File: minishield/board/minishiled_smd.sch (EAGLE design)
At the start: 13 parts, among them CON1 TWIG-90-SMD, CON2 TWIG-90-SMD, U1 ARDUINO_SHIELDNO_SILK

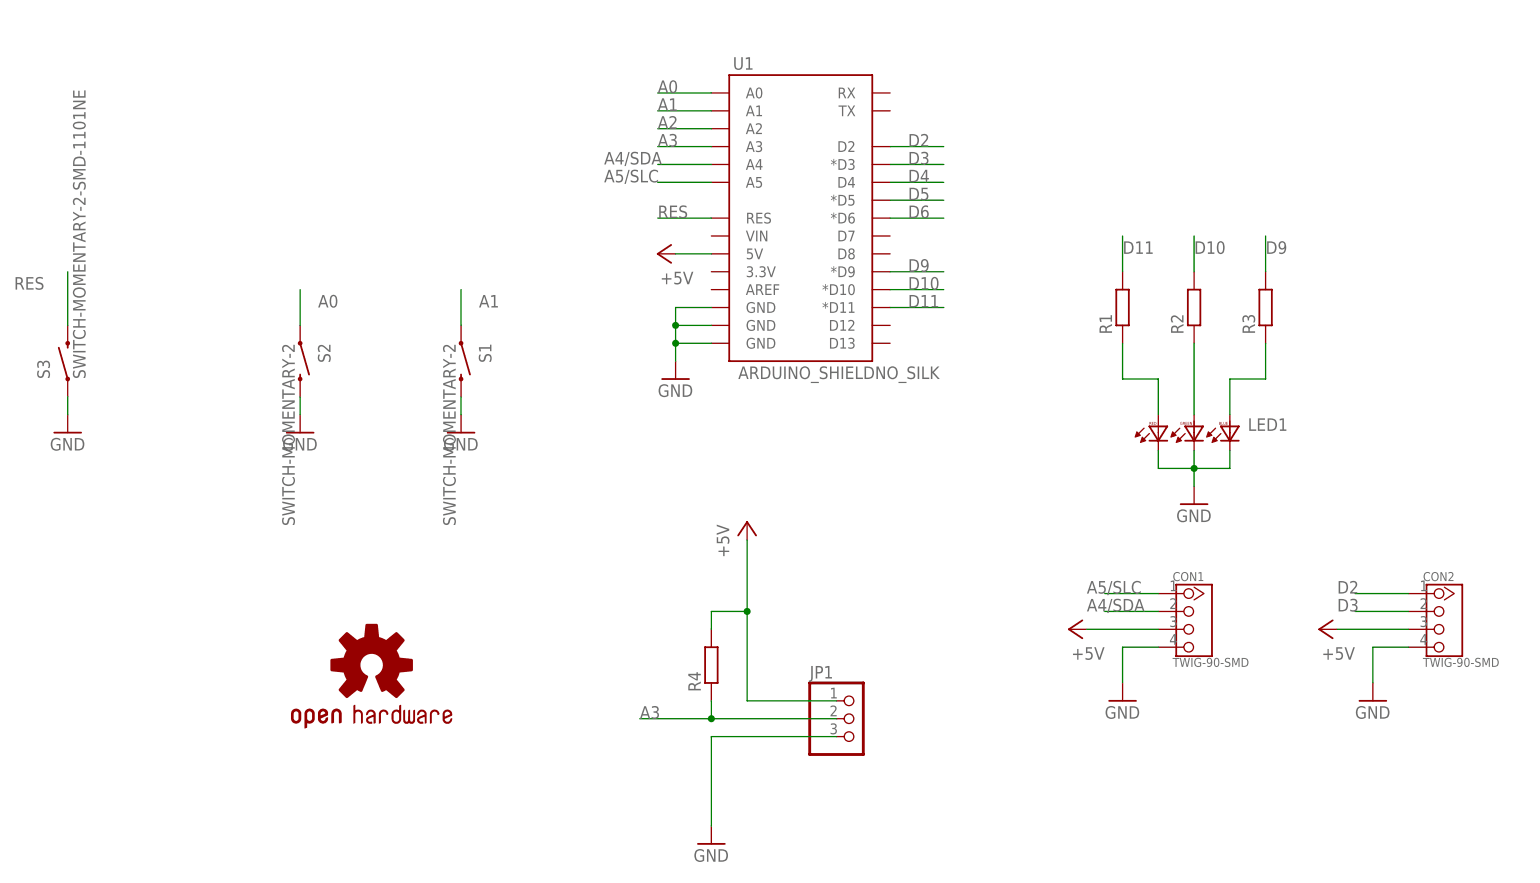
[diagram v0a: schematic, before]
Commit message: Add extension port tests.
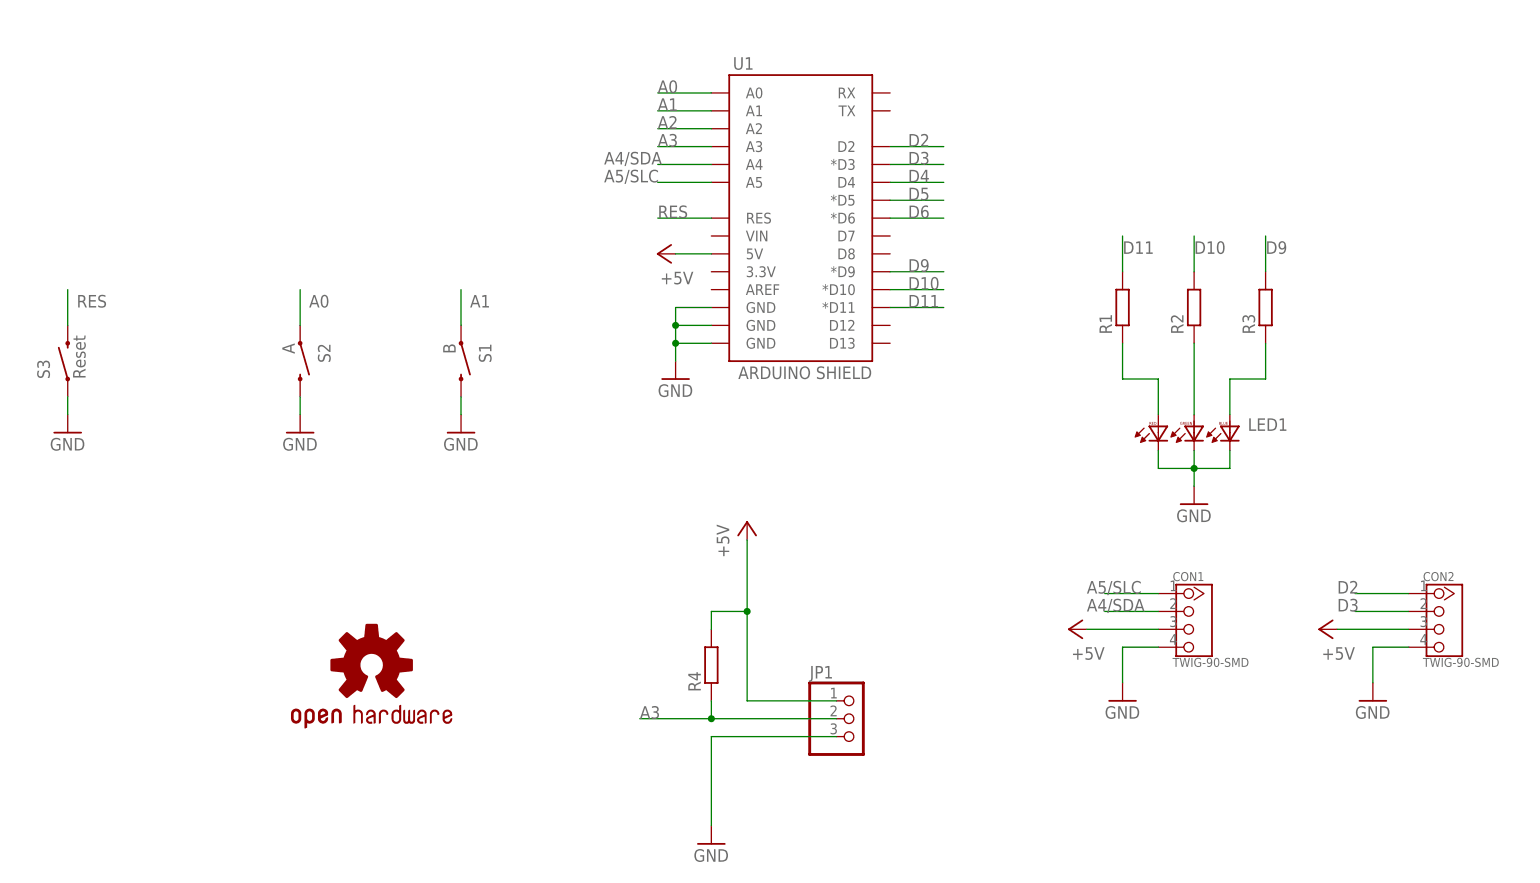
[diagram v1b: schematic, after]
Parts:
- S1: value SWITCH-MOMENTARY-2 -> B
- S2: value SWITCH-MOMENTARY-2 -> A
- S3: value SWITCH-MOMENTARY-2-SMD-1101NE -> Reset
- U1: value ARDUINO_SHIELDNO_SILK -> ARDUINO SHIELD
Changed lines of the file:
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@@
 <setting verticaltext="up"/>
 </settings>
-<grid distance="0.1" unitdist="inch" unit="inch" style="lines" multiple="1" display="no" altdistance="0.01" altunitdist="inch" altunit="inch"/>
+<grid distance="0.1" unitdist="inch" unit="inch" style="lines" multiple="1" display="no" altdistance="0.05" altunitdist="inch" altunit="inch"/>
 <layers>
 <layer number="1" name="Top" color="4" fill="1" visible="no" active="no"/>
@@
 </classes>
 <parts>
-<part name="U1" library="SparkFun-Boards" deviceset="ARDUINO_SHIELD" device="NO_SILK"/>
+<part name="U1" library="SparkFun-Boards" deviceset="ARDUINO_SHIELD" device="NO_SILK" value="ARDUINO SHIELD"/>
 <part name="GND1" library="supply1" deviceset="GND" device=""/>
 <part name="P+1" library="supply1" deviceset="+5V" device=""/>
@@
 <part name="R3" library="rcl" deviceset="R-EU_" device="R1206"/>
 <part name="GND2" library="supply1" deviceset="GND" device=""/>
-<part name="S1" library="SparkFun-Electromechanical" deviceset="SWITCH-MOMENTARY-2" device=""/>
+<part name="S1" library="SparkFun-Electromechanical" deviceset="SWITCH-MOMENTARY-2" device="" value="B"/>
 <part name="GND3" library="supply1" deviceset="GND" device=""/>
-<part name="S2" library="SparkFun-Electromechanical" deviceset="SWITCH-MOMENTARY-2" device=""/>
+<part name="S2" library="SparkFun-Electromechanical" deviceset="SWITCH-MOMENTARY-2" device="" value="A"/>
 <part name="GND4" library="supply1" deviceset="GND" device=""/>
 <part name="P+4" library="supply1" deviceset="+5V" device=""/>
 <part name="GND5" library="supply1" deviceset="GND" device=""/>
-<part name="S3" library="SparkFun-Electromechanical" deviceset="SWITCH-MOMENTARY-2" device="-SMD-1101NE"/>
+<part name="S3" library="SparkFun-Electromechanical" deviceset="SWITCH-MOMENTARY-2" device="-SMD-1101NE" value="Reset"/>
 <part name="GND6" library="supply1" deviceset="GND" device=""/>
 <part name="GND7" library="supply1" deviceset="GND" device=""/>
@@
 <pinref part="S2" gate="G$1" pin="1"/>
 <wire x1="-10.16" y1="48.26" x2="-10.16" y2="53.34" width="0.1524" layer="91"/>
-<label x="-7.62" y="50.8" size="1.778" layer="95"/>
+<label x="-8.89" y="50.8" size="1.778" layer="95"/>
 </segment>
 </net>
@@
 <pinref part="S1" gate="G$1" pin="1"/>
 <wire x1="12.7" y1="48.26" x2="12.7" y2="53.34" width="0.1524" layer="91"/>
-<label x="15.24" y="50.8" size="1.778" layer="95"/>
+<label x="13.97" y="50.8" size="1.778" layer="95"/>
 </segment>
 </net>
@@
 <segment>
 <pinref part="S3" gate="G$1" pin="2"/>
-<wire x1="-43.18" y1="48.26" x2="-43.18" y2="55.88" width="0.1524" layer="91"/>
-<label x="-50.8" y="53.34" size="1.778" layer="95"/>
-</segment>
-</net>
+<wire x1="-43.18" y1="48.26" x2="-43.18" y2="53.34" width="0.1524" layer="91"/>
+<label x="-41.91" y="50.8" size="1.778" layer="95"/>
+</segment>
+</net>
